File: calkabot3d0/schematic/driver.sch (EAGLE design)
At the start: 56 parts

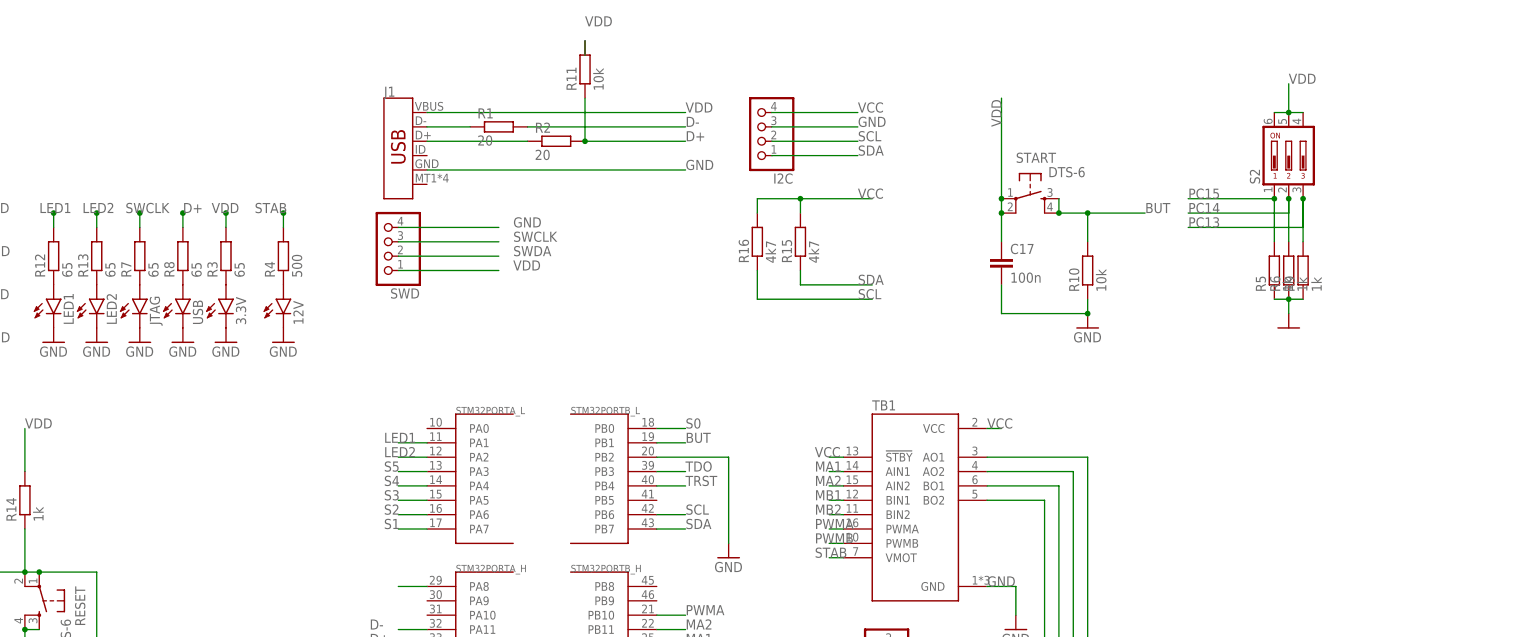
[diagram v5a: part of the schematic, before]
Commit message: added battery voltage checker and led
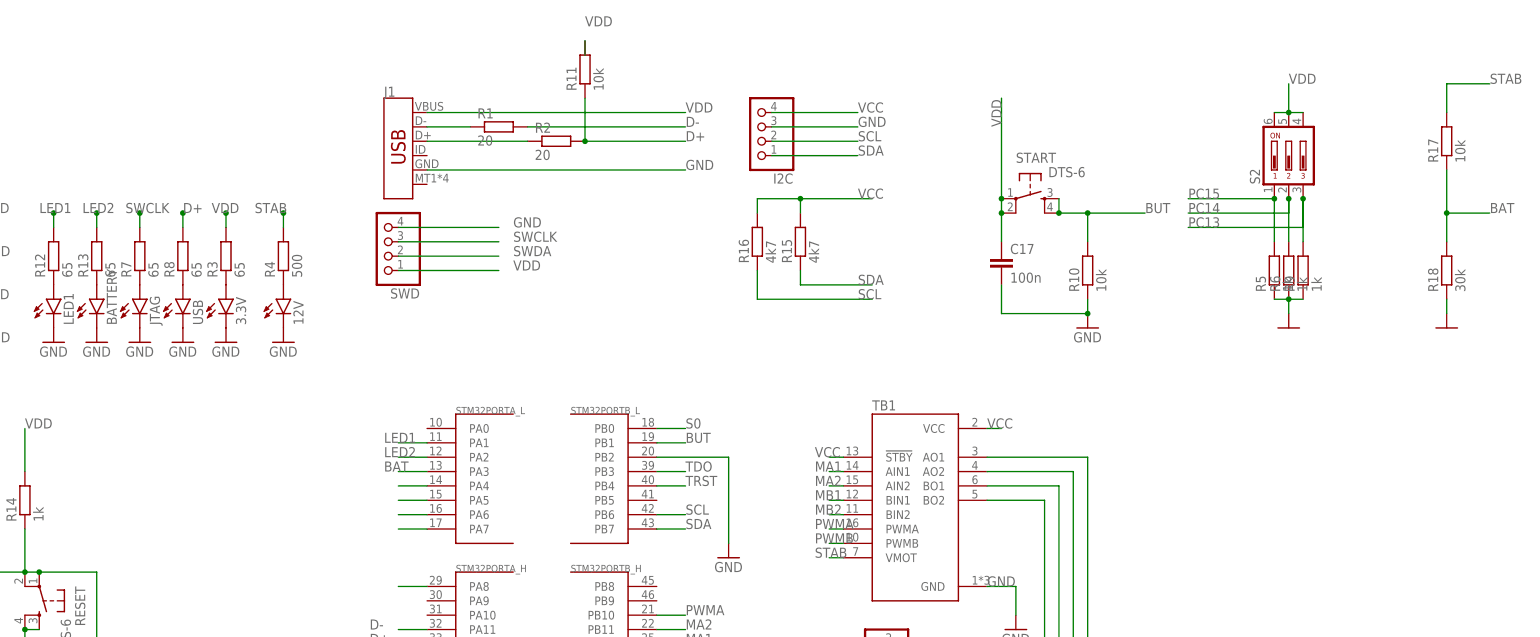
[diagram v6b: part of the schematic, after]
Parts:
- added R17: 10k, rcl:R-EU_R0805
- added R18: 30k, rcl:R-EU_R0805
- renumbered LED2 to BATTERY
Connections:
- removed net S5: STM32PORTA_L.PA3
- new net BAT: R17.1, R18.2, STM32PORTA_L.PA3
- net GND: now also R18.1
- net STAB: now also R17.2
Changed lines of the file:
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@@
 <attribute name="SPICEPREFIX" value="D"/>
 </part>
-<part name="LED2" library="led" library_urn="urn:adsk.eagle:library:259" deviceset="LED" device="CHIPLED_0805" package3d_urn="urn:adsk.eagle:package:15821/2" override_package3d_urn="urn:adsk.eagle:package:17628446/2" override_package_urn="urn:adsk.eagle:footprint:15685/1" override_locally_modified="yes">
+<part name="BATTERY" library="led" library_urn="urn:adsk.eagle:library:259" deviceset="LED" device="CHIPLED_0805" package3d_urn="urn:adsk.eagle:package:15821/2" override_package3d_urn="urn:adsk.eagle:package:17628446/2" override_package_urn="urn:adsk.eagle:footprint:15685/1" override_locally_modified="yes">
 <attribute name="SPICEPREFIX" value="D"/>
 </part>
@@
 <part name="JP5" library="pinhead" library_urn="urn:adsk.eagle:library:325" deviceset="PINHD-1X2" device="/90" package3d_urn="urn:adsk.eagle:package:22437/2"/>
 <part name="GND15" library="supply1" library_urn="urn:adsk.eagle:library:371" deviceset="GND" device=""/>
+<part name="R17" library="rcl" library_urn="urn:adsk.eagle:library:334" deviceset="R-EU_" device="R0805" package3d_urn="urn:adsk.eagle:package:23553/2" value="10k"/>
+<part name="R18" library="rcl" library_urn="urn:adsk.eagle:library:334" deviceset="R-EU_" device="R0805" package3d_urn="urn:adsk.eagle:package:23553/2" value="30k"/>
+<part name="GND21" library="supply1" library_urn="urn:adsk.eagle:library:371" deviceset="GND" device=""/>
 </parts>
 <sheets>
@@
 <attribute name="VALUE" x="-159.385" y="81.788" size="1.778" layer="96" rot="R90"/>
 </instance>
-<instance part="LED2" gate="G$1" x="-157.48" y="86.36" smashed="yes">
+<instance part="BATTERY" gate="G$1" x="-157.48" y="86.36" smashed="yes">
 <attribute name="NAME" x="-153.924" y="81.788" size="1.778" layer="95" rot="R90"/>
 <attribute name="VALUE" x="-151.765" y="81.788" size="1.778" layer="96" rot="R90"/>
@@
 <attribute name="VALUE" x="2.54" y="25.4" size="1.778" layer="96"/>
 </instance>
+<instance part="R17" gate="G$1" x="81.28" y="114.3" smashed="yes" rot="R90">
+<attribute name="NAME" x="79.7814" y="110.49" size="1.778" layer="95" rot="R90"/>
+<attribute name="VALUE" x="84.582" y="110.49" size="1.778" layer="96" rot="R90"/>
+</instance>
+<instance part="R18" gate="G$1" x="81.28" y="91.44" smashed="yes" rot="R90">
+<attribute name="NAME" x="79.7814" y="87.63" size="1.778" layer="95" rot="R90"/>
+<attribute name="VALUE" x="84.582" y="87.63" size="1.778" layer="96" rot="R90"/>
+</instance>
+<instance part="GND21" gate="1" x="81.28" y="81.28" smashed="yes"/>
 </instances>
 <busses>
@@
 </segment>
 <segment>
-<pinref part="LED2" gate="G$1" pin="C"/>
+<pinref part="BATTERY" gate="G$1" pin="C"/>
 <pinref part="GND9" gate="1" pin="GND"/>
 </segment>
@@
 <pinref part="USB" gate="G$1" pin="C"/>
 <pinref part="GND7" gate="1" pin="GND"/>
+</segment>
+<segment>
+<pinref part="R18" gate="G$1" pin="1"/>
+<pinref part="GND21" gate="1" pin="GND"/>
+<wire x1="81.28" y1="86.36" x2="81.28" y2="83.82" width="0.1524" layer="91"/>
 </segment>
 </net>
@@
 <pinref part="C18" gate="G$1" pin="+"/>
 </segment>
+<segment>
+<pinref part="R17" gate="G$1" pin="2"/>
+<wire x1="81.28" y1="119.38" x2="81.28" y2="124.46" width="0.1524" layer="91"/>
+<wire x1="81.28" y1="124.46" x2="88.9" y2="124.46" width="0.1524" layer="91"/>
+<label x="88.9" y="124.46" size="1.778" layer="95"/>
+</segment>
 </net>
 <net name="LED1" class="0">
@@
 <pinref part="STM32" gate="PORTA_L" pin="PA7"/>
 <wire x1="-99.06" y1="45.72" x2="-104.14" y2="45.72" width="0.1524" layer="91"/>
-<label x="-106.68" y="45.72" size="1.778" layer="95"/>
 </segment>
 </net>
@@
 <pinref part="STM32" gate="PORTA_L" pin="PA6"/>
 <wire x1="-99.06" y1="48.26" x2="-104.14" y2="48.26" width="0.1524" layer="91"/>
-<label x="-106.68" y="48.26" size="1.778" layer="95"/>
 </segment>
 </net>
@@
 <pinref part="STM32" gate="PORTA_L" pin="PA5"/>
 <wire x1="-99.06" y1="50.8" x2="-104.14" y2="50.8" width="0.1524" layer="91"/>
-<label x="-106.68" y="50.8" size="1.778" layer="95"/>
 </segment>
 </net>
@@
 <pinref part="STM32" gate="PORTA_L" pin="PA4"/>
 <wire x1="-99.06" y1="53.34" x2="-104.14" y2="53.34" width="0.1524" layer="91"/>
-<label x="-106.68" y="53.34" size="1.778" layer="95"/>
-</segment>
-</net>
-<net name="S5" class="0">
+</segment>
+</net>
+<net name="BAT" class="0">
 <segment>
 <pinref part="STM32" gate="PORTA_L" pin="PA3"/>
@@
 <label x="-106.68" y="55.88" size="1.778" layer="95"/>
 </segment>
+<segment>
+<pinref part="R17" gate="G$1" pin="1"/>
+<pinref part="R18" gate="G$1" pin="2"/>
+<wire x1="81.28" y1="109.22" x2="81.28" y2="101.6" width="0.1524" layer="91"/>
+<wire x1="81.28" y1="101.6" x2="81.28" y2="96.52" width="0.1524" layer="91"/>
+<wire x1="81.28" y1="101.6" x2="88.9" y2="101.6" width="0.1524" layer="91"/>
+<junction x="81.28" y="101.6"/>
+<label x="88.9" y="101.6" size="1.778" layer="95"/>
+</segment>
 </net>
 <net name="SWDA" class="0">
@@
 <net name="N$8" class="0">
 <segment>
-<pinref part="LED2" gate="G$1" pin="A"/>
+<pinref part="BATTERY" gate="G$1" pin="A"/>
 <pinref part="R13" gate="G$1" pin="1"/>
 </segment>

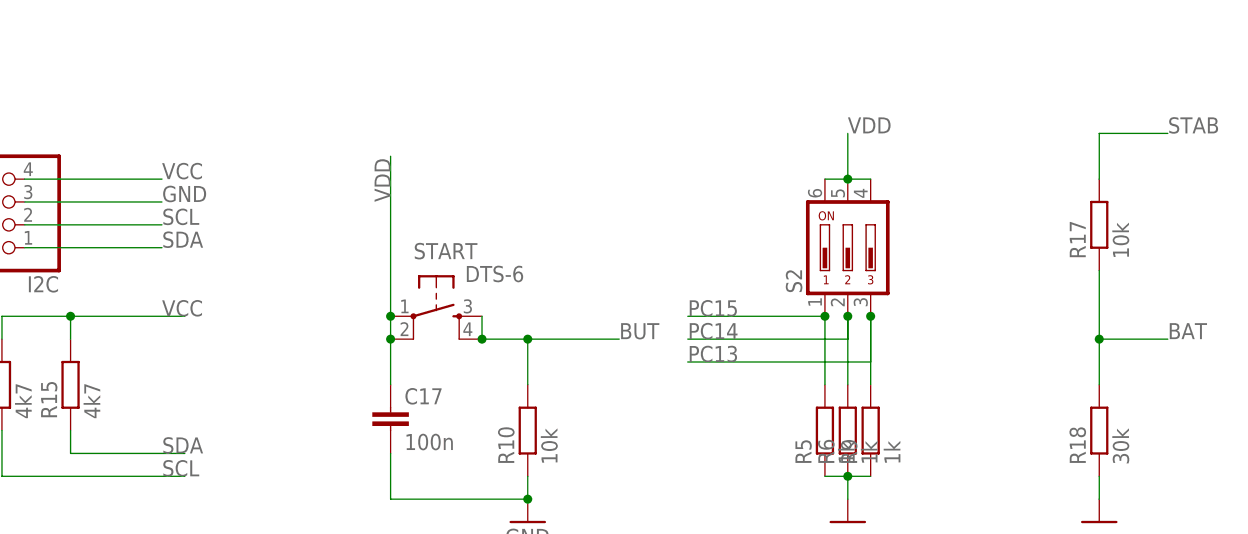
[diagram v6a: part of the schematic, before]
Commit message: added switch to disconnect voltage from sensors
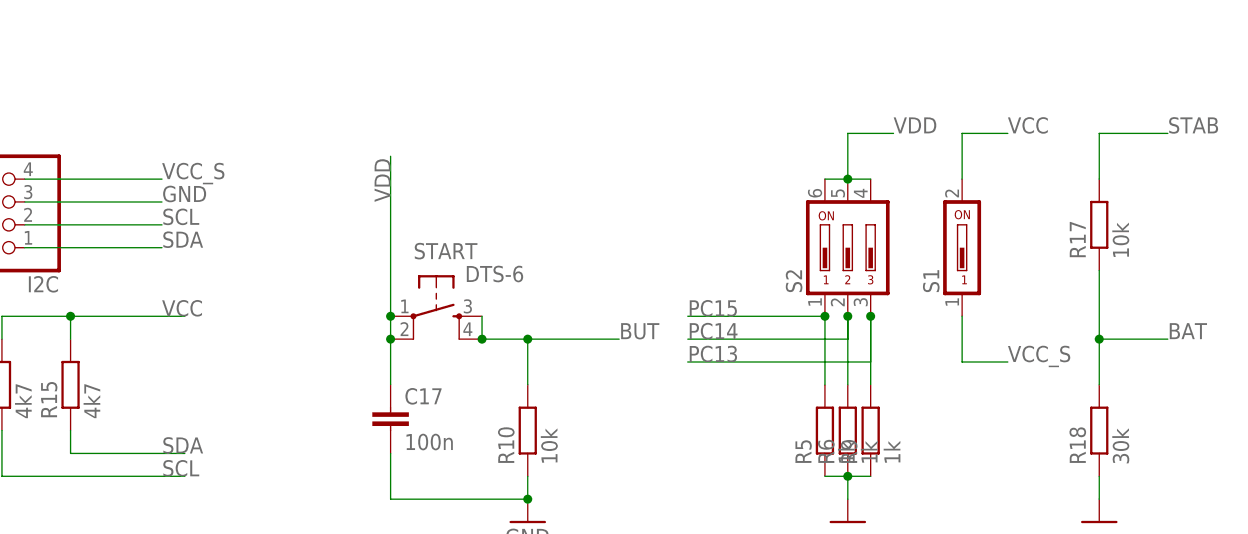
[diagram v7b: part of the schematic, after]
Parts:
- added S1: (no value), switch-dil:SD4-01
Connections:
- new net VCC_S: I2C.4, S1.1
- net VCC: now also S1.2; no longer I2C.4
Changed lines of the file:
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@@
 <part name="R18" library="rcl" library_urn="urn:adsk.eagle:library:334" deviceset="R-EU_" device="R0805" package3d_urn="urn:adsk.eagle:package:23553/2" value="30k"/>
 <part name="GND21" library="supply1" library_urn="urn:adsk.eagle:library:371" deviceset="GND" device=""/>
+<part name="S1" library="switch-dil" library_urn="urn:adsk.eagle:library:375" deviceset="SD4-01" device="" package3d_urn="urn:adsk.eagle:package:27236/1"/>
 </parts>
 <sheets>
@@
 </instance>
 <instance part="GND21" gate="1" x="81.28" y="81.28" smashed="yes"/>
+<instance part="S1" gate="1" x="66.04" y="111.76" smashed="yes">
+<attribute name="NAME" x="63.5" y="106.68" size="1.778" layer="95" rot="R90"/>
+<attribute name="VALUE" x="70.485" y="106.68" size="1.778" layer="96" rot="R90"/>
+</instance>
 </instances>
 <busses>
@@
 <junction x="53.34" y="119.38"/>
 <wire x1="53.34" y1="119.38" x2="53.34" y2="124.46" width="0.1524" layer="91"/>
-<label x="53.34" y="124.46" size="1.778" layer="95"/>
+<label x="58.42" y="124.46" size="1.778" layer="95"/>
+<wire x1="53.34" y1="124.46" x2="58.42" y2="124.46" width="0.1524" layer="91"/>
 </segment>
 <segment>
@@
 </segment>
 <segment>
-<pinref part="I2C" gate="A" pin="4"/>
-<wire x1="-38.1" y1="119.38" x2="-22.86" y2="119.38" width="0.1524" layer="91"/>
-<label x="-22.86" y="119.38" size="1.778" layer="95"/>
-</segment>
-<segment>
 <pinref part="R16" gate="G$1" pin="2"/>
 <wire x1="-40.64" y1="101.6" x2="-40.64" y2="104.14" width="0.1524" layer="91"/>
@@
 <label x="-22.86" y="104.14" size="1.778" layer="95"/>
 </segment>
+<segment>
+<pinref part="S1" gate="1" pin="2"/>
+<wire x1="66.04" y1="119.38" x2="66.04" y2="124.46" width="0.1524" layer="91"/>
+<label x="71.12" y="124.46" size="1.778" layer="95"/>
+<wire x1="66.04" y1="124.46" x2="71.12" y2="124.46" width="0.1524" layer="91"/>
+</segment>
 </net>
 <net name="N$42" class="0">
@@
 </segment>
 </net>
+<net name="VCC_S" class="0">
+<segment>
+<pinref part="S1" gate="1" pin="1"/>
+<wire x1="66.04" y1="104.14" x2="66.04" y2="99.06" width="0.1524" layer="91"/>
+<wire x1="66.04" y1="99.06" x2="71.12" y2="99.06" width="0.1524" layer="91"/>
+<label x="71.12" y="99.06" size="1.778" layer="95"/>
+</segment>
+<segment>
+<pinref part="I2C" gate="A" pin="4"/>
+<wire x1="-38.1" y1="119.38" x2="-22.86" y2="119.38" width="0.1524" layer="91"/>
+<label x="-22.86" y="119.38" size="1.778" layer="95"/>
+</segment>
+</net>

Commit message: comments on schematic, added led for I2C supply
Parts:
- added BATTERY1: (no value), led:LEDCHIPLED_0805
- added R19: 65, rcl:R-EU_R0805
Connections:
- new net N$9: BATTERY1.A, R19.1
- net GND: now also BATTERY1.C
- net VCC_S: now also R19.2
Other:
- note added: "Ledy informacyjne"
- note added: "Zasilanie'"
- note added: "komunikacje"
- note added: "mikrokontroler"
- note added: "mikrokontroler I/O"
- note added: "przełączniki"
- note added: "sterownik silników"
- moved on the sheet: 12V, 3.3V, BATTERY, C10, C11, C15, C16, C9, J1, JP4, JP5, JTAG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
